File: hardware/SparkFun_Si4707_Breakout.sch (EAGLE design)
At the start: 40 parts, among them J3 OUTPUT, J4 ANT, U3 TPA6111, Y1 32.768kHz

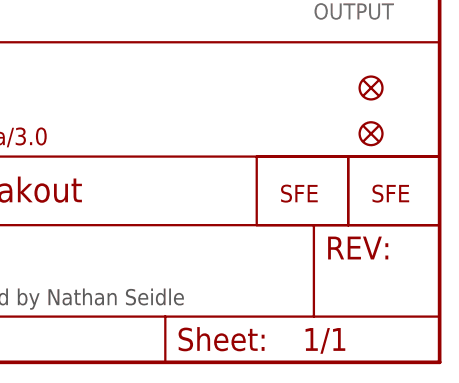
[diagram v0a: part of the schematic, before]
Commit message: Updating directory structure, adding version to hardware files, updating readme
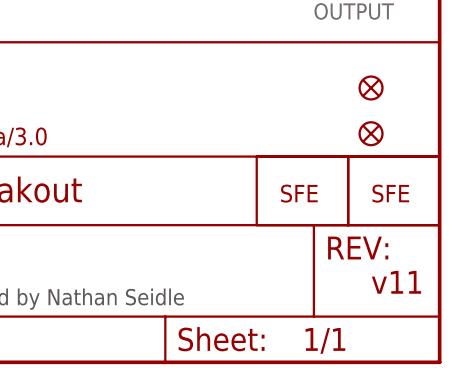
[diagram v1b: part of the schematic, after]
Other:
- note added: "v11"
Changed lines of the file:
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@@
 <?xml version="1.0" encoding="utf-8"?>
 <!DOCTYPE eagle SYSTEM "eagle.dtd">
-<eagle version="6.4">
+<eagle version="7.2.0">
 <drawing>
 <settings>
@@
 <layer number="254" name="cooling" color="7" fill="1" visible="no" active="yes"/>
 </layers>
-<schematic xreflabel="%F%N/%S.%C%R" xrefpart="/%S.%C%R">
+<schematic xreflabel="%F%N/%S" xrefpart="/%S">
 <attributes>
 </attributes>
@@
 the audio jack must be green-
 wire fixed to ground.</text>
+<text x="241.3" y="7.62" size="2.54" layer="94">v11</text>
 </plain>
 <instances>
